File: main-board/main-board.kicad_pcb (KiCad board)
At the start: 2 copper layers, 210 x 130 mm, 174 parts, among them J1 PWR_SELECT, J10 Conn_02x05_Odd_Even, J11 Conn_02x05_Odd_Even, J12 Conn_02x05_Odd_Even, J13 Conn_02x05_Odd_Even, J14 Conn_02x05_Odd_Even, J15 Conn_02x05_Odd_Even, J16 COMM_3, J17 Modular board connector, J18 PWR_EXT_1, J19 PWR_EXT_2, J2 COMM1, J20 COMM_4, J21 COMM_OUT, J3 ICSP, J4 Conn_02x03_Top_Bottom, J5 COMM_2, J7 Conn_02x05_Odd_Even, J8 Conn_02x05_Odd_Even, J9 Conn_02x05_Odd_Even, SW1 RESET, SW10 SW_Push, SW11 SW_Push, SW12 SW_SP3T_x08, SW13 SW_Push, SW14 SW_Push, SW15 SW_Push, SW16 SW_Push, SW17 SW_Push, SW18 SW_Push, SW19 SW_Push, SW2 BTN_LEVEL, SW20 SW_Push, SW21 SW_SP3T_x08, SW22 SW_Push, SW23 SW_Push, SW24 SW_Push, SW25 SW_Push, SW26 SW_Push, SW27 SW_Push, SW28 SW_Push, SW29 SW_Push, SW3 LED_GND, SW30 SW_SP3T_x08, SW31 SW_Push, SW32 SW_Push, SW33 SW_Push, SW34 SW_Push, SW35 SW_Push, SW36 SW_Push, SW37 SW_Push, SW38 SW_Push, SW39 SW_SP3T_x08, SW4 SW_Push, SW41 PWR_EN, SW5 SW_Push, SW6 SW_Push, SW7 SW_Push, SW8 SW_Push, SW9 SW_Push, U1 LM2576HVS-5, U2 AP1117-33, U3 AP1117-18, U4 FT232RL

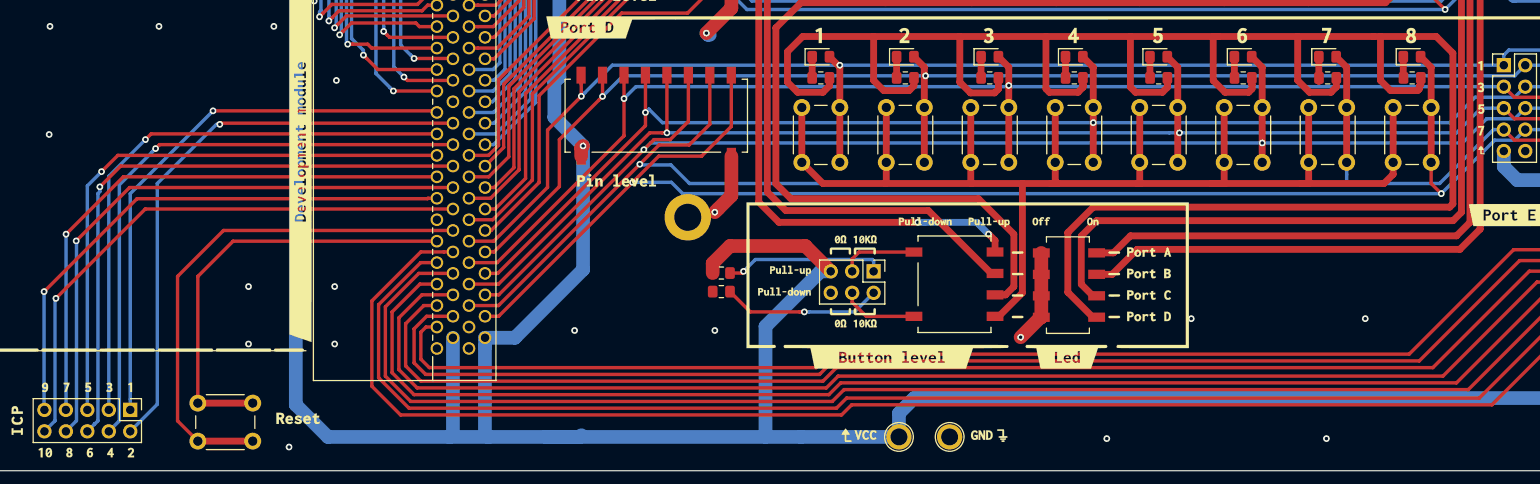
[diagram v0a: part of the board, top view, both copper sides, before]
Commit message: Added QBoard logos
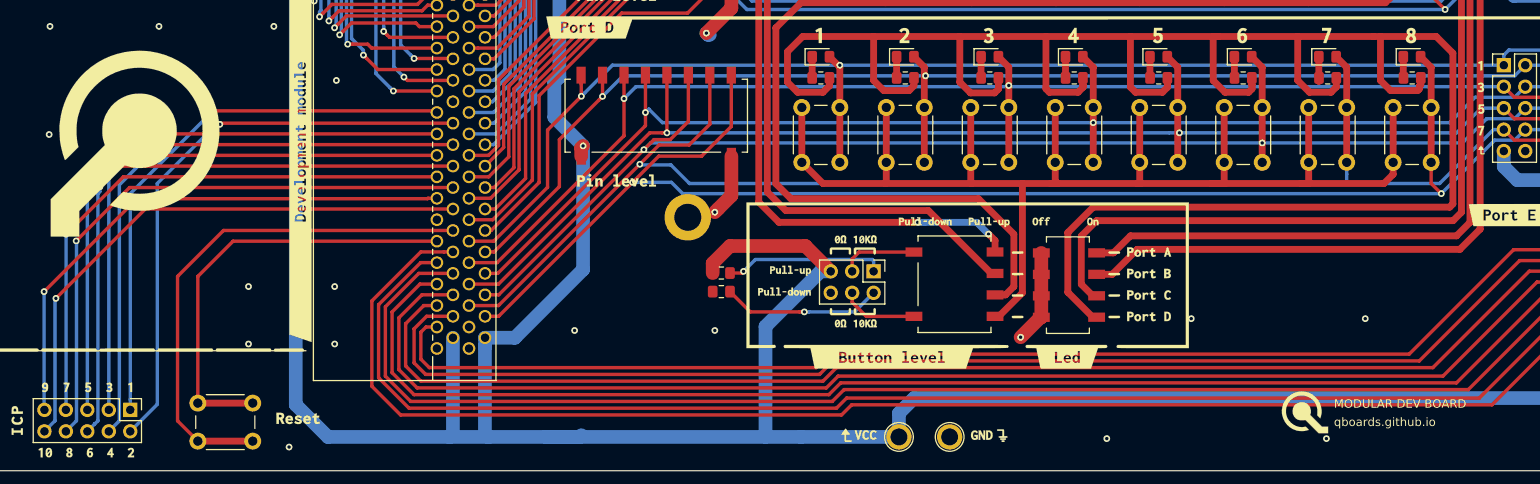
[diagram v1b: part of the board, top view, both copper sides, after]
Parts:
- added MODULAR DEV BOARD: LOGO_BRD_REF, qboards_aesthetics:logo_url-5mm, F.Cu at (204.7, 141.0)
- added MODULAR DEV BOARD v1.0: LOGO_BRD_REF, qboards_aesthetics:logo_url-5mm, B.Cu at (210.1, 140.3)
- added [BRD_REF]: LOGO_BRD_REF, qboards_aesthetics:logo-20mm, F.Cu at (67.0, 107.8)

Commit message: Fixed revision number
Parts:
- MODULAR DEV BOARD | Rev 1.0: renamed from MODULAR DEV BOARD v1.0
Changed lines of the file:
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@@
   )
   (layers
-    (0 F.Cu signal)
-    (31 B.Cu signal)
-    (32 B.Adhes user)
-    (33 F.Adhes user)
+    (0 F.Cu signal hide)
+    (31 B.Cu signal hide)
+    (32 B.Adhes user hide)
+    (33 F.Adhes user hide)
     (34 B.Paste user)
-    (35 F.Paste user)
+    (35 F.Paste user hide)
     (36 B.SilkS user)
-    (37 F.SilkS user)
+    (37 F.SilkS user hide)
     (38 B.Mask user)
-    (39 F.Mask user)
-    (40 Dwgs.User user)
-    (41 Cmts.User user)
-    (42 Eco1.User user)
-    (43 Eco2.User user)
+    (39 F.Mask user hide)
+    (40 Dwgs.User user hide)
+    (41 Cmts.User user hide)
+    (42 Eco1.User user hide)
+    (43 Eco2.User user hide)
     (44 Edge.Cuts user)
-    (45 Margin user)
+    (45 Margin user hide)
     (46 B.CrtYd user)
-    (47 F.CrtYd user)
+    (47 F.CrtYd user hide)
     (48 B.Fab user)
-    (49 F.Fab user)
+    (49 F.Fab user hide)
   )
   (setup
@@
   (module qboards_aesthetics:logo_url-5mm (layer B.Cu)
     (at 210.1 140.3 180)
-    (fp_text reference "MODULAR DEV BOARD v1.0" (at 3.7846 0.9144) (layer B.SilkS)
+    (fp_text reference "MODULAR DEV BOARD | Rev 1.0" (at 3.7846 0.9144) (layer B.SilkS)
       (effects (font (size 1 1) (thickness 0.18)) (justify left mirror))
     )

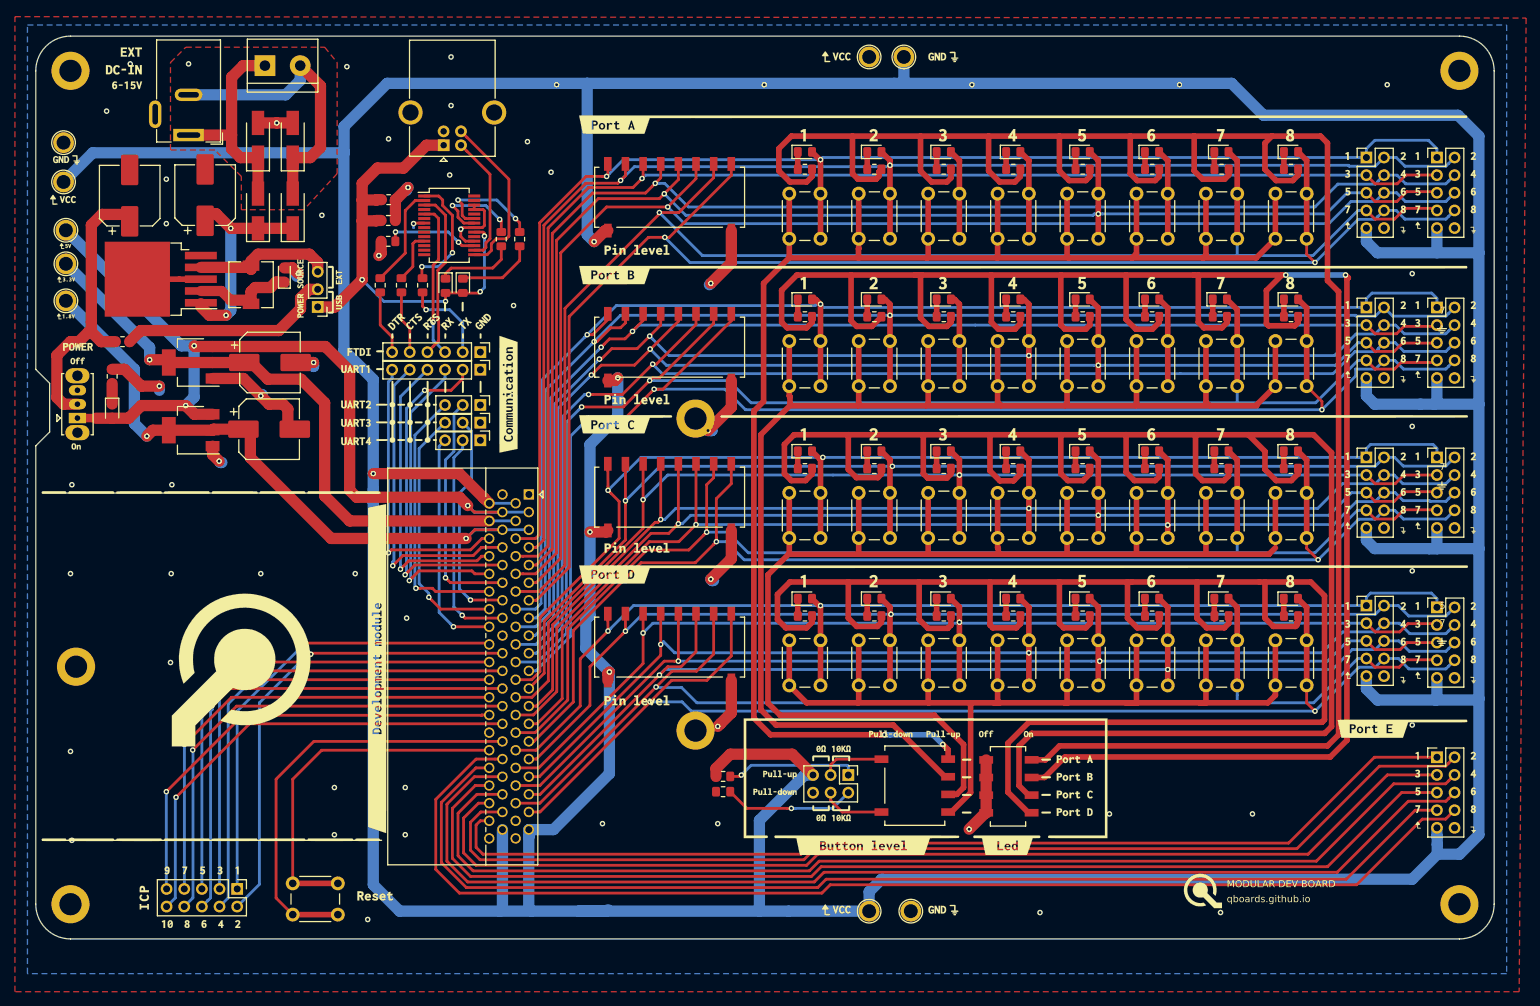
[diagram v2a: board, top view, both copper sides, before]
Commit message: Fixed top test point mislabeling
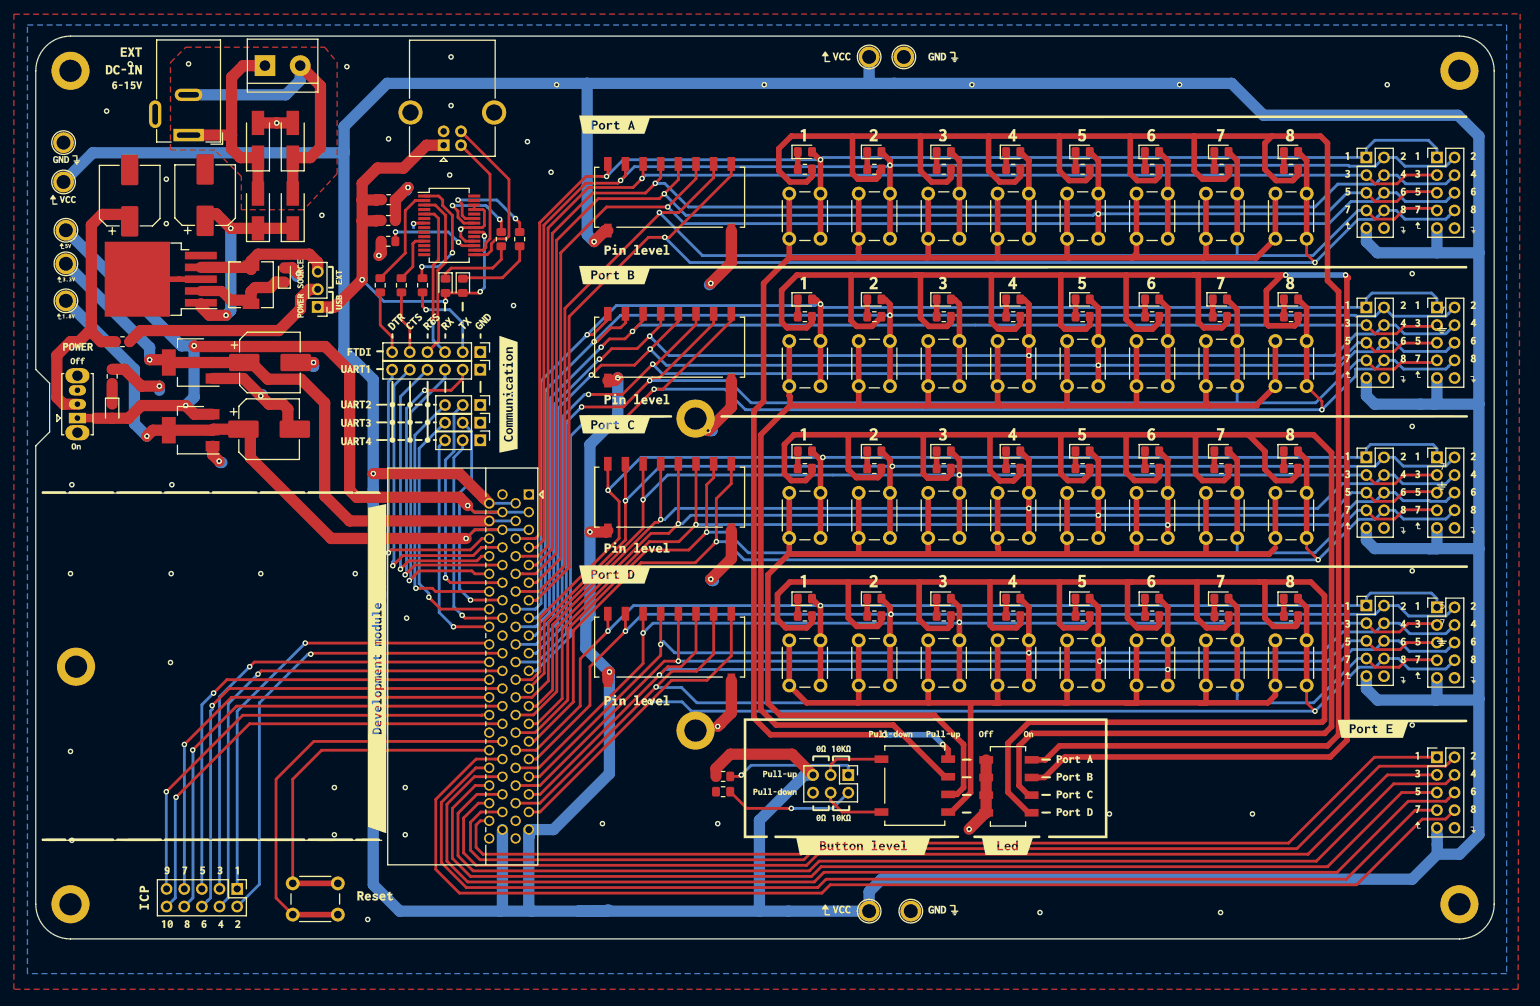
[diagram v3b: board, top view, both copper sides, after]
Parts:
- removed MODULAR DEV BOARD: LOGO_BRD_REF, qboards_aesthetics:logo_url-5mm
- removed MODULAR DEV BOARD | Rev 1.0: LOGO_BRD_REF, qboards_aesthetics:logo_url-5mm
- removed [BRD_REF]: LOGO_BRD_REF, qboards_aesthetics:logo-20mm
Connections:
- TP_GND3 pad 1: GND -> VBUS
- TP_VBUS2 pad 1: VBUS -> GND

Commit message: Updated/fixed Qboards references
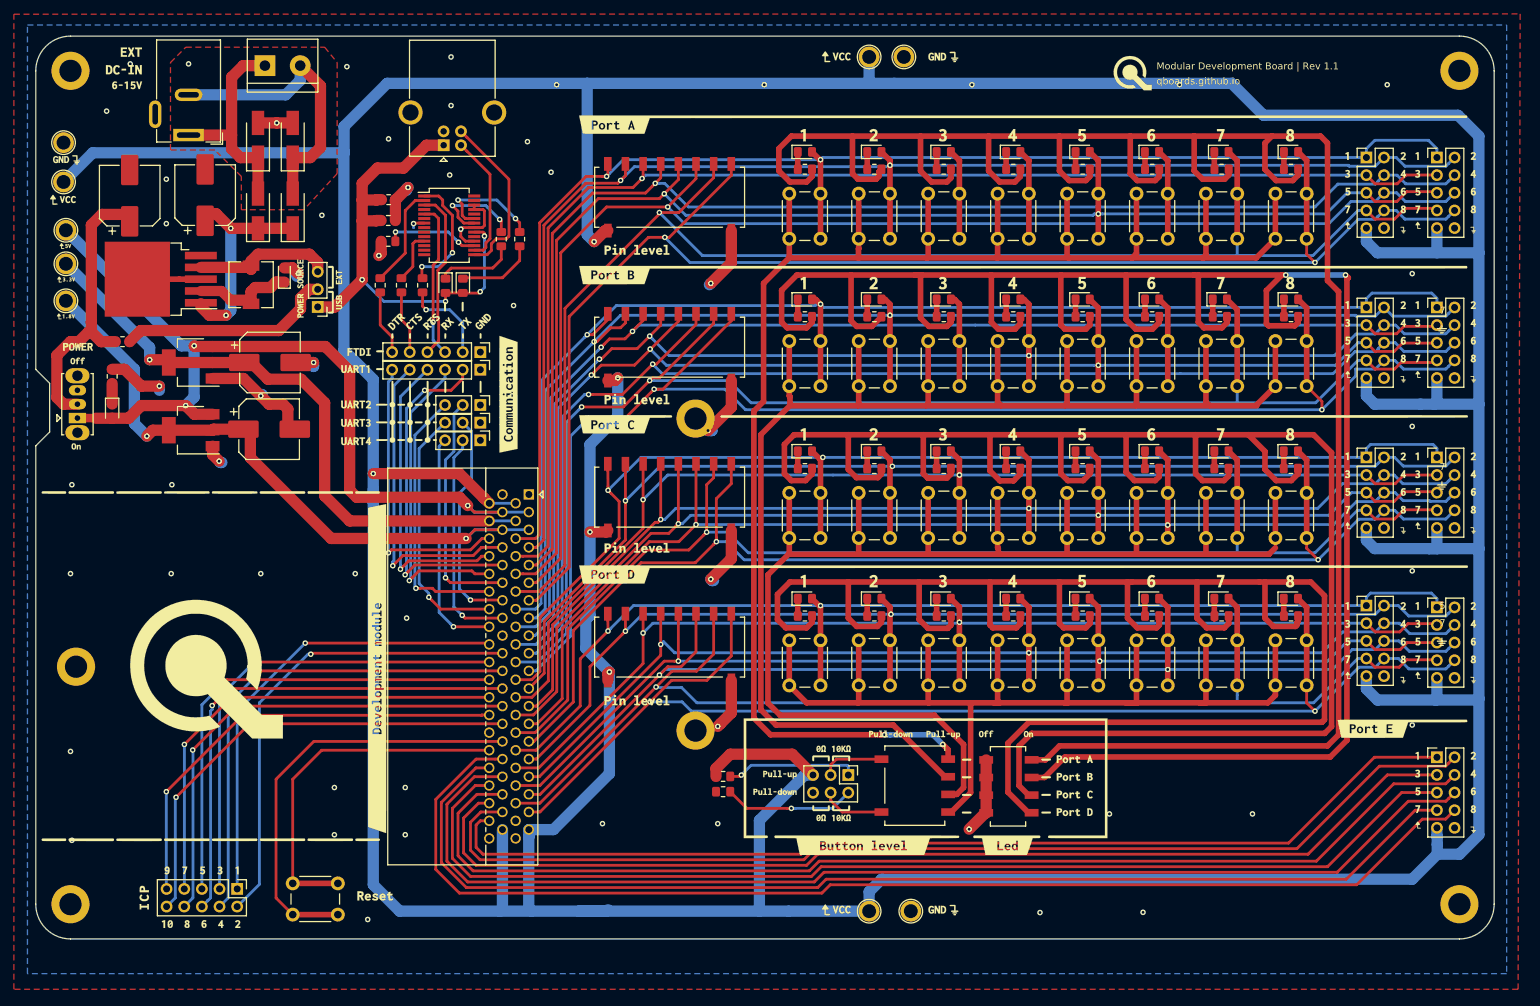
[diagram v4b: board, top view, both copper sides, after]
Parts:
- added Modular Development Board | Rev 1.1: LOGO_BRD_REF, qboards_aesthetics:logo_url-5mm, F.Cu at (194.6, 23.2)
- added [BRD_REF]: LOGO_BRD_REF, qboards_aesthetics:logo-20mm, F.Cu at (60.1, 108.7)

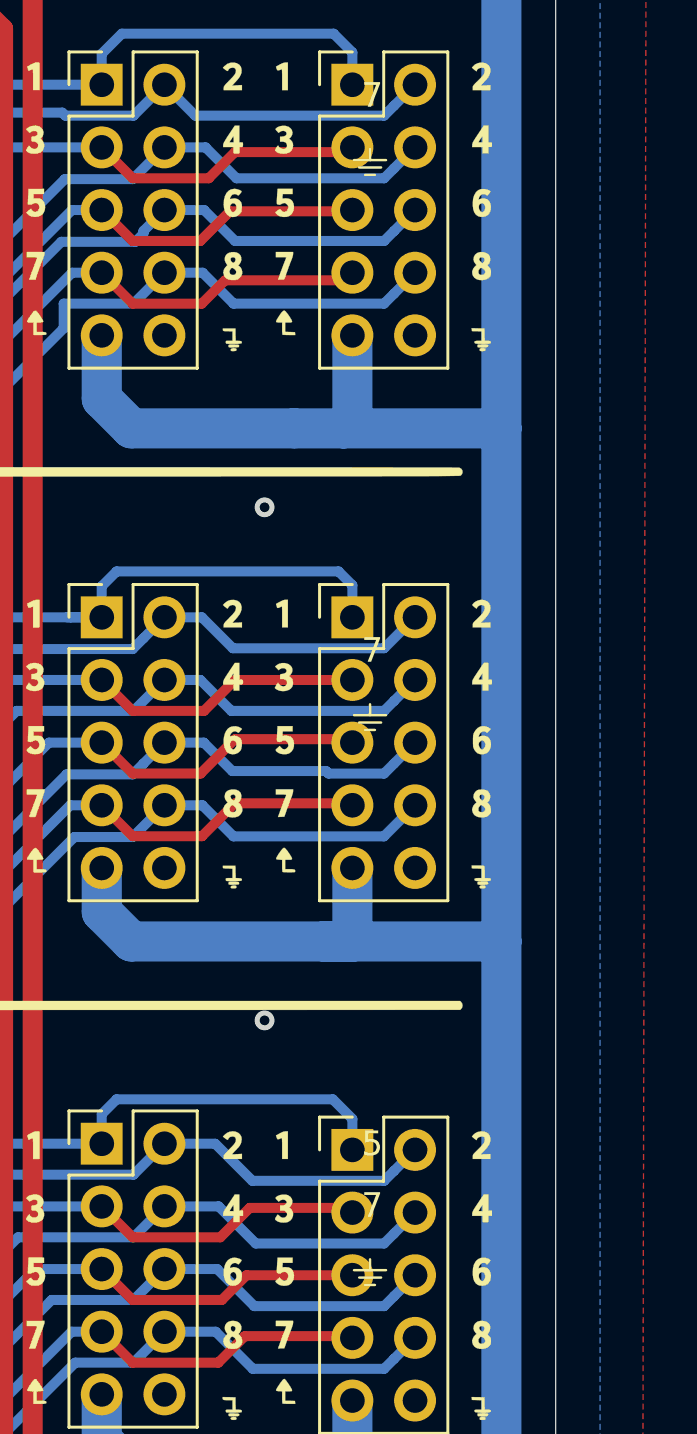
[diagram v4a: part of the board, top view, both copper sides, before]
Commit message: Clarified R4,5,6 value, tidied F.SilkS and F,Fab
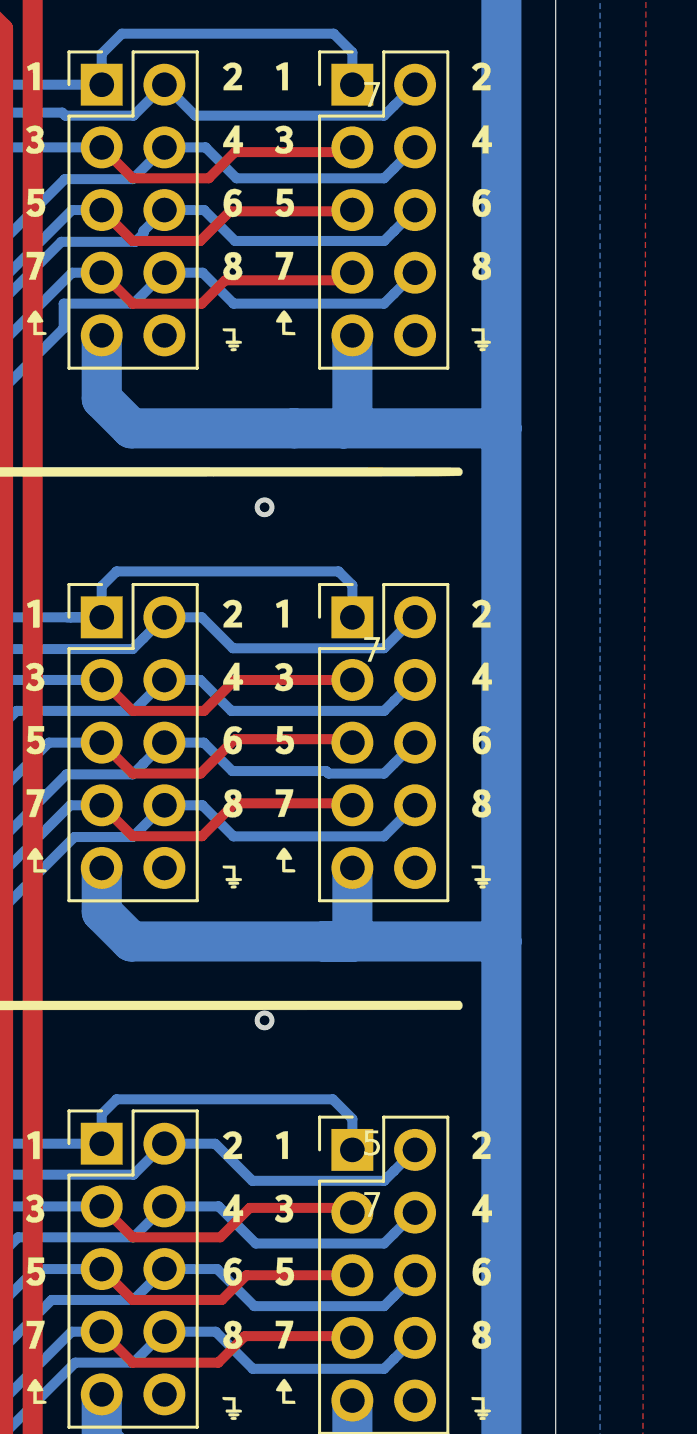
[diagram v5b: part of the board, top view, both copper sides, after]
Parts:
- removed REF** (x3): gnd-symbol, qboards_aesthetics:gnd-symbol
- TP_GND3: value GND -> VBUS
- TP_VBUS2: value VBUS -> GND
